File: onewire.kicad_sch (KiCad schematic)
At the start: 8 parts, among them J801 Conn_01x03, U801 RCLAMP0524P-N

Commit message: Rename Ferrite_Bead to FerriteBead
Symbol name changed between KiCad 5 and 6...
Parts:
- FB801: symbol Device:Ferrite_Bead -> Device:FerriteBead
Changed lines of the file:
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@@
     (pin "2")
   )
-  (symbol (lib_id "Device:Ferrite_Bead") (at 118.11 99.06 90) (mirror x) (unit 1)
+  (symbol (lib_id "Device:FerriteBead") (at 118.11 99.06 90) (mirror x) (unit 1)
     (in_bom yes) (on_board yes)
     (property "Reference" "FB801" (id 0) (at 118.11 92.1004 90))

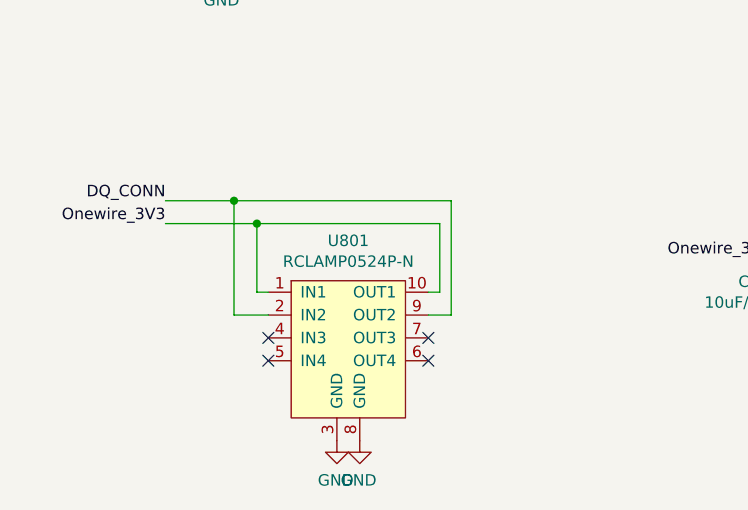
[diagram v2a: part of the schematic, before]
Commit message: Only use the edge signal pins of RCLAMPs if possible
This improves resiliency to slight misalignment during manufacturing.
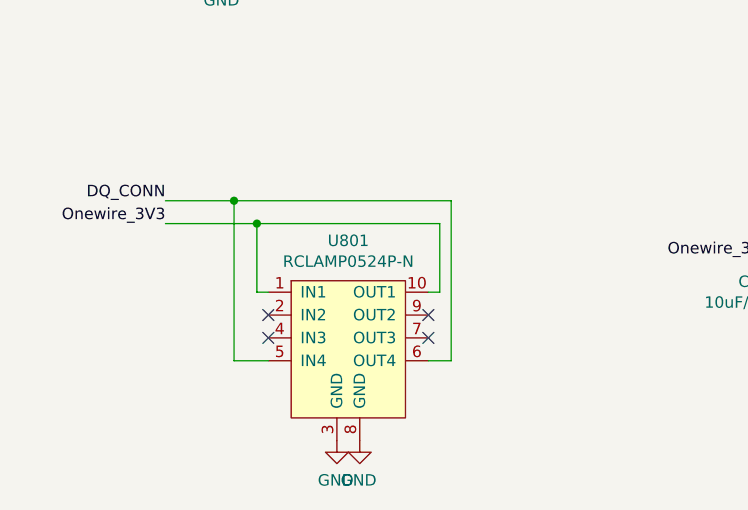
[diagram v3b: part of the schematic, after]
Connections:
- net DQ_CONN: now also U801.5 (IN4), U801.6 (OUT4); no longer U801.2 (IN2), U801.9 (OUT2)
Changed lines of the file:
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@@
   (junction (at 113.03 99.06) (diameter 0) (color 0 0 0 0)
   )
-  (no_connect (at 53.34 110.49))
   (no_connect (at 53.34 107.95))
-  (no_connect (at 71.12 110.49))
   (no_connect (at 71.12 107.95))
+  (no_connect (at 71.12 105.41))
+  (no_connect (at 53.34 105.41))
   (wire (pts (xy 116.84 59.69) (xy 121.92 59.69))
     (stroke (width 0) (type default) (color 0 0 0 0))
@@
   )
   (wire (pts (xy 116.84 59.69) (xy 116.84 60.96))
-    (stroke (width 0) (type default) (color 0 0 0 0))
-  )
-  (wire (pts (xy 73.66 105.41) (xy 73.66 92.71))
     (stroke (width 0) (type default) (color 0 0 0 0))
   )
@@
     (stroke (width 0) (type default) (color 0 0 0 0))
   )
+  (wire (pts (xy 73.66 92.71) (xy 73.66 110.49))
+    (stroke (width 0) (type default) (color 0 0 0 0))
+  )
   (wire (pts (xy 53.34 102.87) (xy 52.07 102.87))
     (stroke (width 0) (type default) (color 0 0 0 0))
@@
     (stroke (width 0) (type default) (color 0 0 0 0))
   )
-  (wire (pts (xy 49.53 105.41) (xy 49.53 92.71))
+  (wire (pts (xy 49.53 92.71) (xy 49.53 110.49))
     (stroke (width 0) (type default) (color 0 0 0 0))
   )
-  (wire (pts (xy 53.34 105.41) (xy 49.53 105.41))
+  (wire (pts (xy 53.34 110.49) (xy 49.53 110.49))
     (stroke (width 0) (type default) (color 0 0 0 0))
   )
@@
     (stroke (width 0) (type default) (color 0 0 0 0))
   )
-  (wire (pts (xy 71.12 105.41) (xy 73.66 105.41))
+  (wire (pts (xy 71.12 110.49) (xy 73.66 110.49))
     (stroke (width 0) (type default) (color 0 0 0 0))
   )

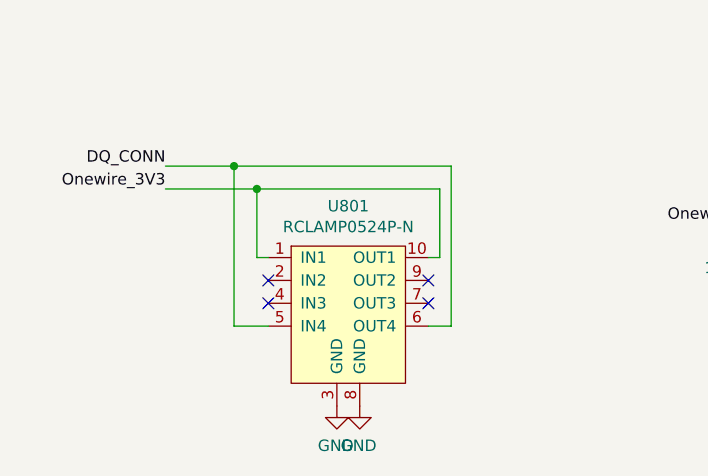
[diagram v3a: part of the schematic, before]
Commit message: Improve connector ESD protection; bump version to 2.0.2
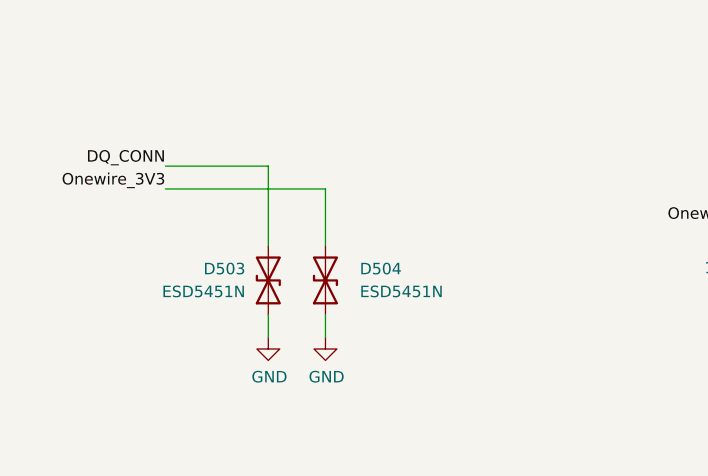
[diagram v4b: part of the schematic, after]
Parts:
- removed U801: RCLAMP0524P-N, Package_DFN_QFN:Diodes_UDFN-10_1.0x2.5mm_P0.5mm, symbol SH-ESP32:RCLAMP0524P-N
- added D503, D504: ESD5451N, Diode_SMD:D_0402_1005Metric, symbol Device:D_TVS
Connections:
- net DQ_CONN: now also D503.2 (A2)
- net GND: now also D503.1 (A1), D504.1 (A1)
- net Onewire_3V3: now also D504.2 (A2)
- no-connect marks 4 -> 0
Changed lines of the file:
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@@
   (title_block
     (title "Sailor Hat with ESP32")
-    (date "2021-12-31")
-    (rev "2.0.1")
+    (date "2022-10-26")
+    (rev "2.0.2")
     (company "Hat Labs Ltd")
     (comment 1 "https://creativecommons.org/licenses/by-sa/4.0")
@@
     (comment 3 "SH-ESP32 is licensed under CC BY-SA 4.0.")
   )
-  (junction (at 49.53 92.71) (diameter 0) (color 0 0 0 0)
-  )
   (junction (at 116.84 59.69) (diameter 0) (color 0 0 0 0)
   )
-  (junction (at 52.07 95.25) (diameter 0) (color 0 0 0 0)
-  )
   (junction (at 123.19 99.06) (diameter 0) (color 0 0 0 0)
   )
   (junction (at 113.03 99.06) (diameter 0) (color 0 0 0 0)
   )
-  (no_connect (at 53.34 107.95))
-  (no_connect (at 71.12 107.95))
-  (no_connect (at 71.12 105.41))
-  (no_connect (at 53.34 105.41))
   (wire (pts (xy 116.84 59.69) (xy 121.92 59.69))
     (stroke (width 0) (type default) (color 0 0 0 0))
@@
     (stroke (width 0) (type default) (color 0 0 0 0))
   )
-  (wire (pts (xy 41.91 92.71) (xy 49.53 92.71))
-    (stroke (width 0) (type default) (color 0 0 0 0))
-  )
-  (wire (pts (xy 52.07 102.87) (xy 52.07 95.25))
+  (wire (pts (xy 41.91 92.71) (xy 53.34 92.71))
     (stroke (width 0) (type default) (color 0 0 0 0))
   )
@@
     (stroke (width 0) (type default) (color 0 0 0 0))
   )
-  (wire (pts (xy 52.07 95.25) (xy 41.91 95.25))
+  (wire (pts (xy 41.91 95.25) (xy 59.69 95.25))
+    (stroke (width 0) (type default) (color 0 0 0 0))
+  )
+  (wire (pts (xy 59.69 109.22) (xy 59.69 111.76))
     (stroke (width 0) (type default) (color 0 0 0 0))
   )
@@
     (stroke (width 0) (type default) (color 0 0 0 0))
   )
-  (wire (pts (xy 72.39 102.87) (xy 72.39 95.25))
-    (stroke (width 0) (type default) (color 0 0 0 0))
-  )
   (wire (pts (xy 121.92 99.06) (xy 123.19 99.06))
     (stroke (width 0) (type default) (color 0 0 0 0))
   )
-  (wire (pts (xy 49.53 92.71) (xy 73.66 92.71))
+  (wire (pts (xy 53.34 92.71) (xy 53.34 101.6))
     (stroke (width 0) (type default) (color 0 0 0 0))
   )
@@
     (stroke (width 0) (type default) (color 0 0 0 0))
   )
+  (wire (pts (xy 59.69 95.25) (xy 59.69 101.6))
+    (stroke (width 0) (type default) (color 0 0 0 0))
+  )
+  (wire (pts (xy 53.34 109.22) (xy 53.34 111.76))
+    (stroke (width 0) (type default) (color 0 0 0 0))
+  )
   (wire (pts (xy 115.57 59.69) (xy 116.84 59.69))
     (stroke (width 0) (type default) (color 0 0 0 0))
   )
-  (wire (pts (xy 73.66 92.71) (xy 73.66 110.49))
-    (stroke (width 0) (type default) (color 0 0 0 0))
-  )
-  (wire (pts (xy 53.34 102.87) (xy 52.07 102.87))
-    (stroke (width 0) (type default) (color 0 0 0 0))
-  )
   (wire (pts (xy 45.72 64.77) (xy 48.26 64.77))
     (stroke (width 0) (type default) (color 0 0 0 0))
   )
-  (wire (pts (xy 72.39 95.25) (xy 52.07 95.25))
-    (stroke (width 0) (type default) (color 0 0 0 0))
-  )
-  (wire (pts (xy 71.12 102.87) (xy 72.39 102.87))
-    (stroke (width 0) (type default) (color 0 0 0 0))
-  )
-  (wire (pts (xy 49.53 92.71) (xy 49.53 110.49))
-    (stroke (width 0) (type default) (color 0 0 0 0))
-  )
-  (wire (pts (xy 53.34 110.49) (xy 49.53 110.49))
-    (stroke (width 0) (type default) (color 0 0 0 0))
-  )
   (wire (pts (xy 123.19 99.06) (xy 127 99.06))
-    (stroke (width 0) (type default) (color 0 0 0 0))
-  )
-  (wire (pts (xy 71.12 110.49) (xy 73.66 110.49))
     (stroke (width 0) (type default) (color 0 0 0 0))
   )
@@
     (pin "1")
   )
-  (symbol (lib_id "SH-ESP32:RCLAMP0524P-N") (at 62.23 107.95 0) (unit 1)
-    (in_bom yes) (on_board yes)
-    (property "Reference" "U801" (id 0) (at 62.23 97.155 0))
-    (property "Value" "RCLAMP0524P-N" (id 1) (at 62.23 99.4664 0))
-    (property "Footprint" "Package_DFN_QFN:Diodes_UDFN-10_1.0x2.5mm_P0.5mm" (id 2) (at 62.23 110.49 0)
-      (effects (font (size 1.27 1.27)) hide)
-    )
-    (property "Datasheet" "" (id 3) (at 62.23 110.49 0)
-      (effects (font (size 1.27 1.27)) hide)
-    )
-    (property "LCSC" "C316044" (id 4) (at 62.23 107.95 0)
-      (effects (font (size 1.27 1.27)) hide)
-    )
-    (pin "1")
-    (pin "10")
-    (pin "2")
-    (pin "3")
-    (pin "4")
-    (pin "5")
-    (pin "6")
-    (pin "7")
-    (pin "8")
-    (pin "9")
-  )
   (symbol (lib_id "power:GND") (at 123.19 106.68 0) (unit 1)
     (in_bom yes) (on_board yes)
@@
     (pin "1")
   )
-  (symbol (lib_id "power:GND") (at 60.96 119.38 0) (mirror y) (unit 1)
-    (in_bom yes) (on_board yes)
-    (property "Reference" "#PWR0803" (id 0) (at 60.96 125.73 0)
-      (effects (font (size 1.27 1.27)) hide)
-    )
-    (property "Value" "GND" (id 1) (at 60.833 123.7742 0))
-    (property "Footprint" "" (id 2) (at 60.96 119.38 0)
-      (effects (font (size 1.27 1.27)) hide)
-    )
-    (property "Datasheet" "" (id 3) (at 60.96 119.38 0)
-      (effects (font (size 1.27 1.27)) hide)
-    )
-    (pin "1")
-  )
-  (symbol (lib_id "power:GND") (at 63.5 119.38 0) (mirror y) (unit 1)
-    (in_bom yes) (on_board yes)
-    (property "Reference" "#PWR0804" (id 0) (at 63.5 125.73 0)
-      (effects (font (size 1.27 1.27)) hide)
-    )
-    (property "Value" "GND" (id 1) (at 63.373 123.7742 0))
-    (property "Footprint" "" (id 2) (at 63.5 119.38 0)
-      (effects (font (size 1.27 1.27)) hide)
-    )
-    (property "Datasheet" "" (id 3) (at 63.5 119.38 0)
-      (effects (font (size 1.27 1.27)) hide)
-    )
+  (symbol (lib_id "Device:D_TVS") (at 59.69 105.41 90) (unit 1)
+    (in_bom yes) (on_board yes)
+    (property "Reference" "D504" (id 0) (at 63.5 104.14 90)
+      (effects (font (size 1.27 1.27)) (justify right))
+    )
+    (property "Value" "ESD5451N" (id 1) (at 63.5 106.68 90)
+      (effects (font (size 1.27 1.27)) (justify right))
+    )
+    (property "Footprint" "Diode_SMD:D_0402_1005Metric" (id 2) (at 59.69 105.41 0)
+      (effects (font (size 1.27 1.27)) hide)
+    )
+    (property "Datasheet" "~" (id 3) (at 59.69 105.41 0)
+      (effects (font (size 1.27 1.27)) hide)
+    )
+    (property "LCSC" "C2936977" (id 4) (at 59.69 105.41 90)
+      (effects (font (size 1.27 1.27)) hide)
+    )
+    (pin "1")
+    (pin "2")
+  )
+  (symbol (lib_id "Device:D_TVS") (at 53.34 105.41 90) (unit 1)
+    (in_bom yes) (on_board yes)
+    (property "Reference" "D503" (id 0) (at 50.8 104.14 90)
+      (effects (font (size 1.27 1.27)) (justify left))
+    )
+    (property "Value" "ESD5451N" (id 1) (at 50.8 106.68 90)
+      (effects (font (size 1.27 1.27)) (justify left))
+    )
+    (property "Footprint" "Diode_SMD:D_0402_1005Metric" (id 2) (at 53.34 105.41 0)
+      (effects (font (size 1.27 1.27)) hide)
+    )
+    (property "Datasheet" "~" (id 3) (at 53.34 105.41 0)
+      (effects (font (size 1.27 1.27)) hide)
+    )
+    (property "LCSC" "C2936977" (id 4) (at 53.34 105.41 90)
+      (effects (font (size 1.27 1.27)) hide)
+    )
+    (pin "1")
+    (pin "2")
+  )
+  (symbol (lib_id "power:GND") (at 59.69 111.76 0) (unit 1)
+    (in_bom yes) (on_board yes)
+    (property "Reference" "#PWR0508" (id 0) (at 59.69 118.11 0)
+      (effects (font (size 1.27 1.27)) hide)
+    )
+    (property "Value" "GND" (id 1) (at 59.817 116.1542 0))
+    (property "Footprint" "" (id 2) (at 59.69 111.76 0)
+      (effects (font (size 1.27 1.27)) hide)
+    )
+    (property "Datasheet" "" (id 3) (at 59.69 111.76 0)
+      (effects (font (size 1.27 1.27)) hide)
+    )
+    (pin "1")
+  )
+  (symbol (lib_id "power:GND") (at 53.34 111.76 0) (unit 1)
+    (in_bom yes) (on_board yes)
+    (property "Reference" "#PWR0507" (id 0) (at 53.34 118.11 0)
+      (effects (font (size 1.27 1.27)) hide)
+    )
+    (property "Value" "GND" (id 1) (at 53.467 116.1542 0))
+    (property "Footprint" "" (id 2) (at 53.34 111.76 0)
+      (effects (font (size 1.27 1.27)) hide)
+    )
+    (property "Datasheet" "" (id 3) (at 53.34 111.76 0)
+      (effects (font (size 1.27 1.27)) hide)
+    )

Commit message: Fix component rotations
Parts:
- J801: JLCPCB_CORRECTION (none) -> 0;2.54;90
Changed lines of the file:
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@@
       (effects (font (size 1.27 1.27)) hide)
     )
-    (property "JLCPCB_CORRECTION" "" (at 40.64 62.23 0)
+    (property "JLCPCB_CORRECTION" "0;2.54;90" (at 40.64 62.23 0)
       (effects (font (size 1.27 1.27)) hide)
     )

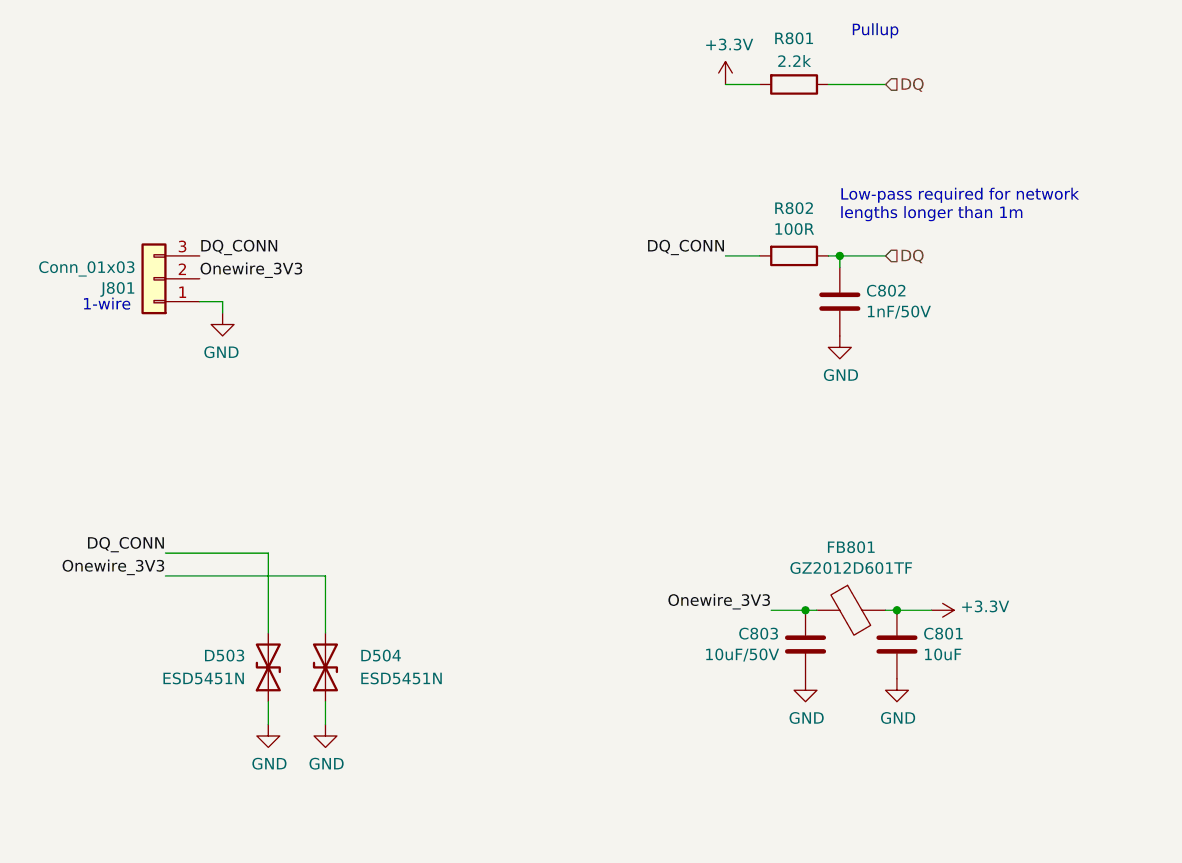
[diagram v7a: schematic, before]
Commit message: Go back to ISO1050 for CAN transceiver
Also add CAN RX and TX LEDs and beef up buck capacitors
as much as space allows.
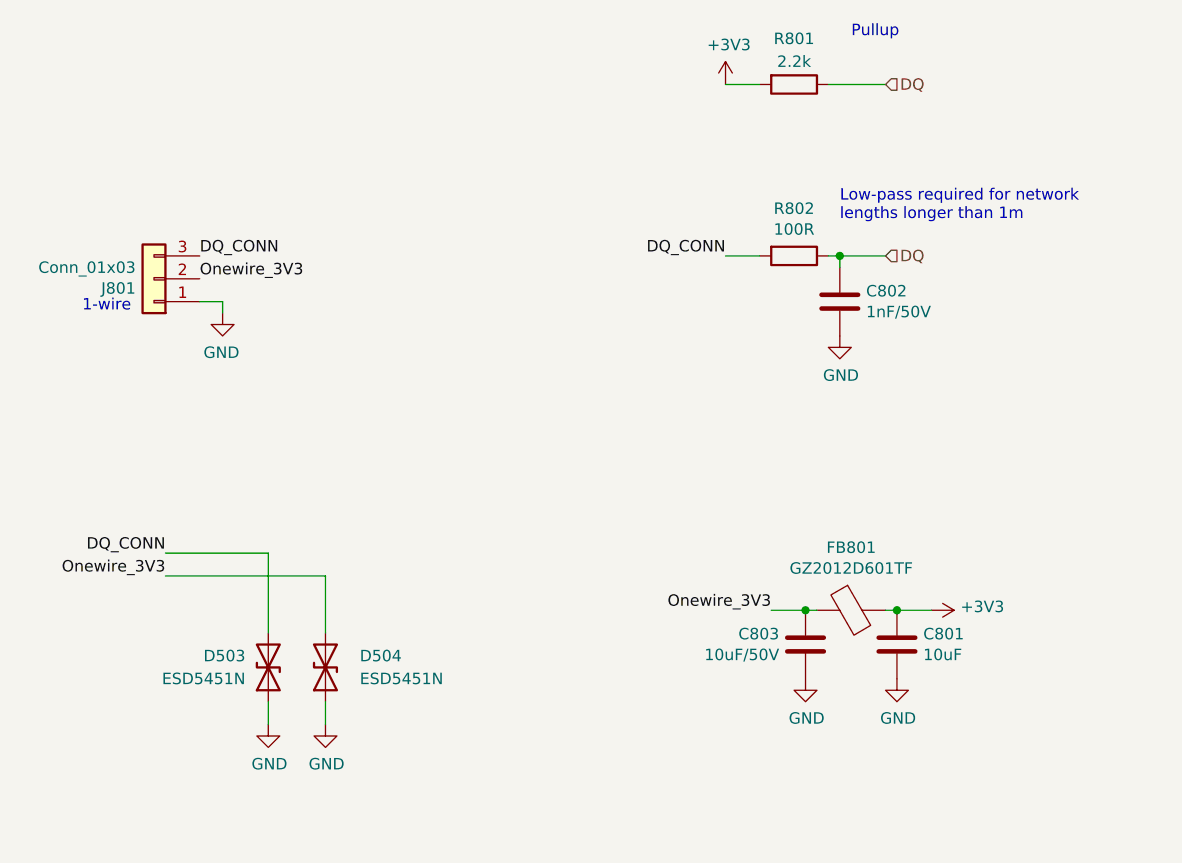
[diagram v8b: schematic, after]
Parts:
- J801: LCSC C49257 -> C6332196
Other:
- company: Hat Labs Ltd -> Hat Labs Oy
- title: Sailor Hat with ESP32 -> SH-ESP32
